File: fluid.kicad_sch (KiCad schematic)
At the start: 28 parts, among them J1 Gate 1, J2 Gate 2, J3 Power, SW1 Button, SW2 Button, U1 TL074, U2 TL074, U3 TL074, U4 TL074

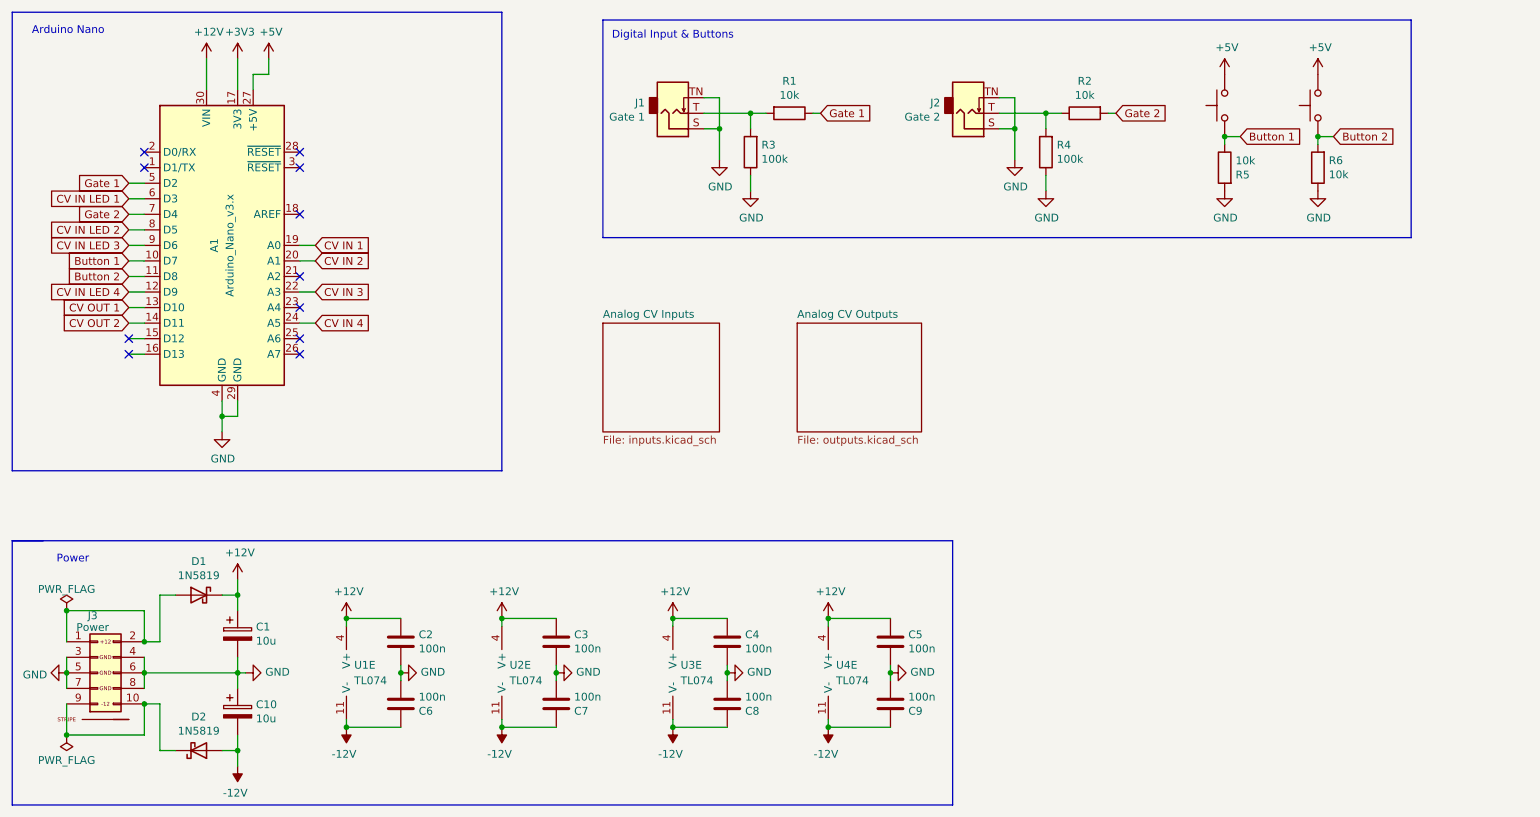
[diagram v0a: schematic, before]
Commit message: Reintroduce the DAC with gain boost from 4.096v to 9.99v. Refactor output LED, increase LED resistor value.
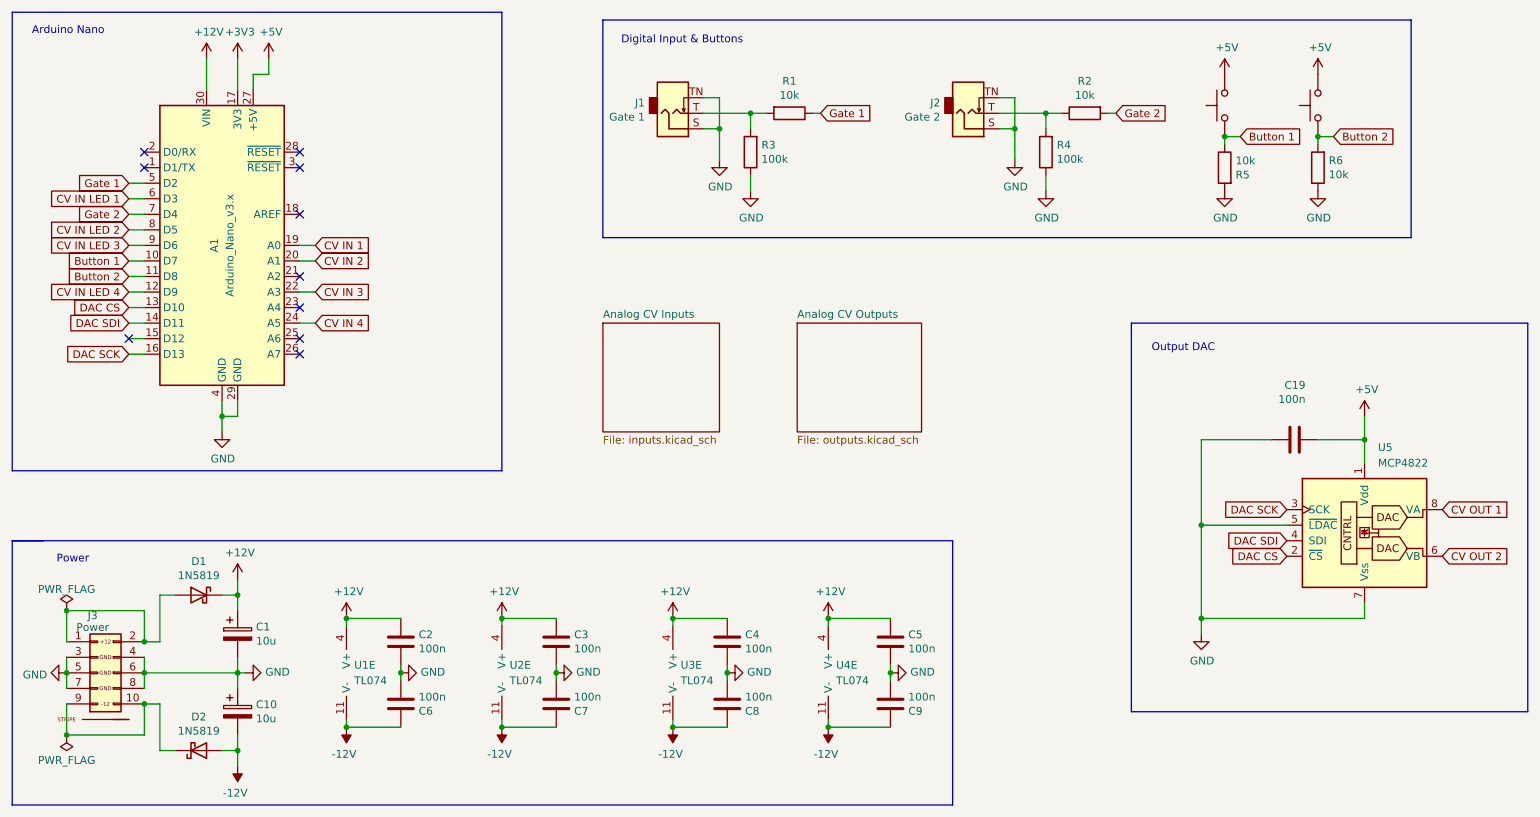
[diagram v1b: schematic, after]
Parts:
- added C19: 100n, Capacitor_SMD:C_0402_1005Metric, symbol Device:C
- added U5: MCP4822, Package_SO:SOIC-8_3.9x4.9mm_P1.27mm, symbol Analog_DAC:MCP4822
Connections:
- net +5V: now also C19.1, U5.1 (Vdd)
- net CV OUT 1: now also U5.8 (VA); no longer A1.13 (D10)
- net CV OUT 2: now also U5.6 (VB); no longer A1.14 (D11)
- net GND: now also C19.2, U5.5 (~{LDAC}), U5.7 (Vss)
- net DAC SCK: now reaches A1.16 (D13)
- net DAC SCK: now also U5.3 (SCK)
- new net DAC CS: A1.13 (D10), U5.2 (~{CS})
- new net DAC SDI: A1.14 (D11), U5.4 (SDI)
- no-connect marks 11 -> 10
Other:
- note added: "Output DAC"

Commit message: reorder annotations, replot pdf schematic
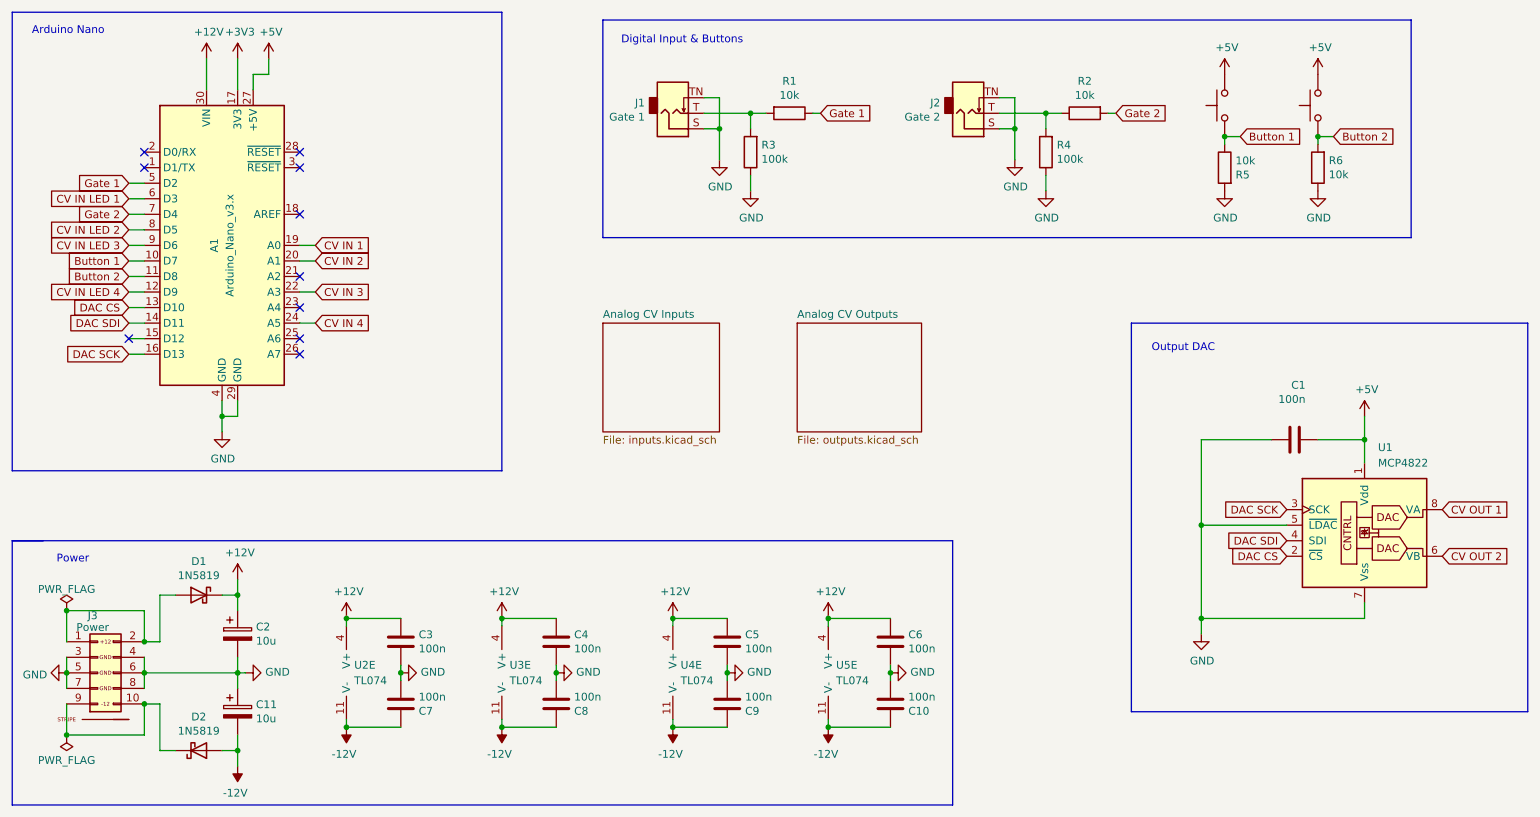
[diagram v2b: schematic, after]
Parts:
- renumbered C19 to C1, C9 to C10, C10 to C11, C1 to C2, C2 to C3, C3 to C4, C4 to C5, C5 to C6, C6 to C7, C7 to C8, C8 to C9, U5 to U1, U1 to U2, U2 to U3, U3 to U4, U4 to U5
